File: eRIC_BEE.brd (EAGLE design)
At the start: 25.2 x 34 mm, 40 parts

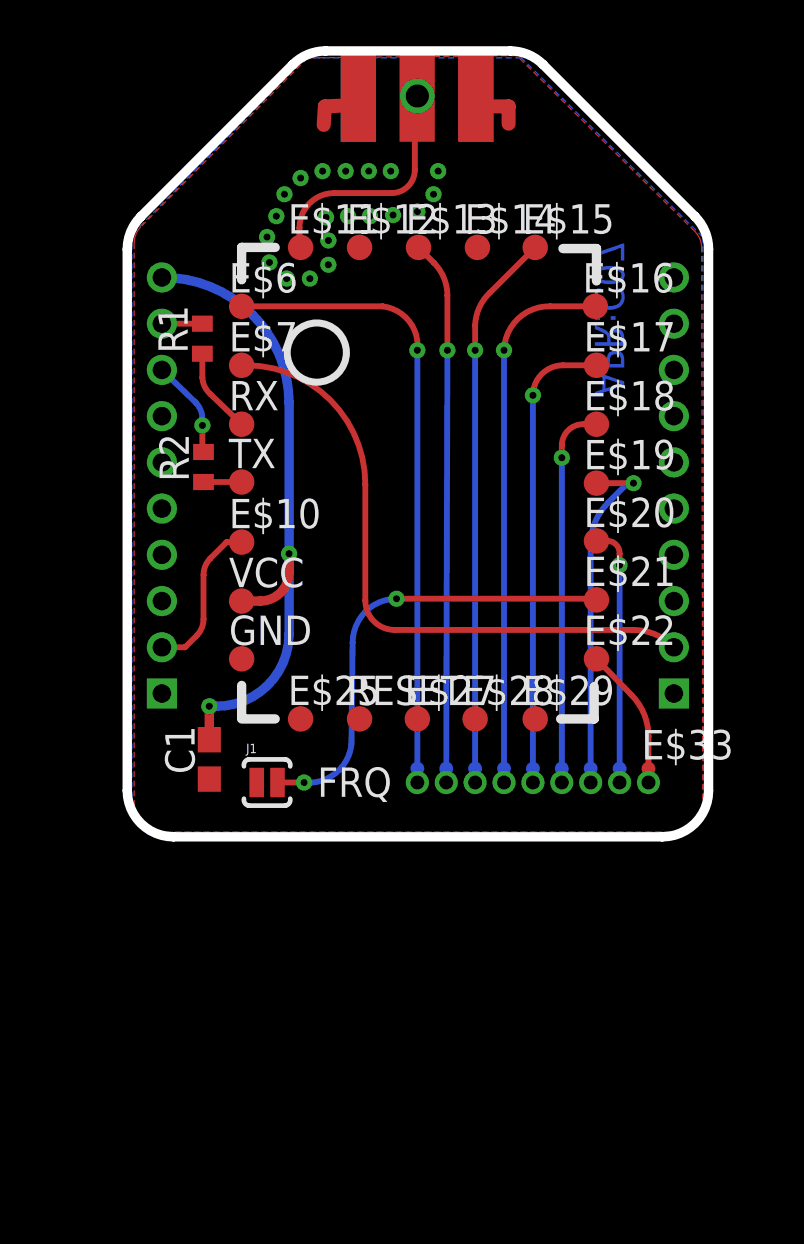
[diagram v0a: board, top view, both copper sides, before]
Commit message: revision 1.8, eagle 7.2 cam, new board design to eliminate need for wonky stitching
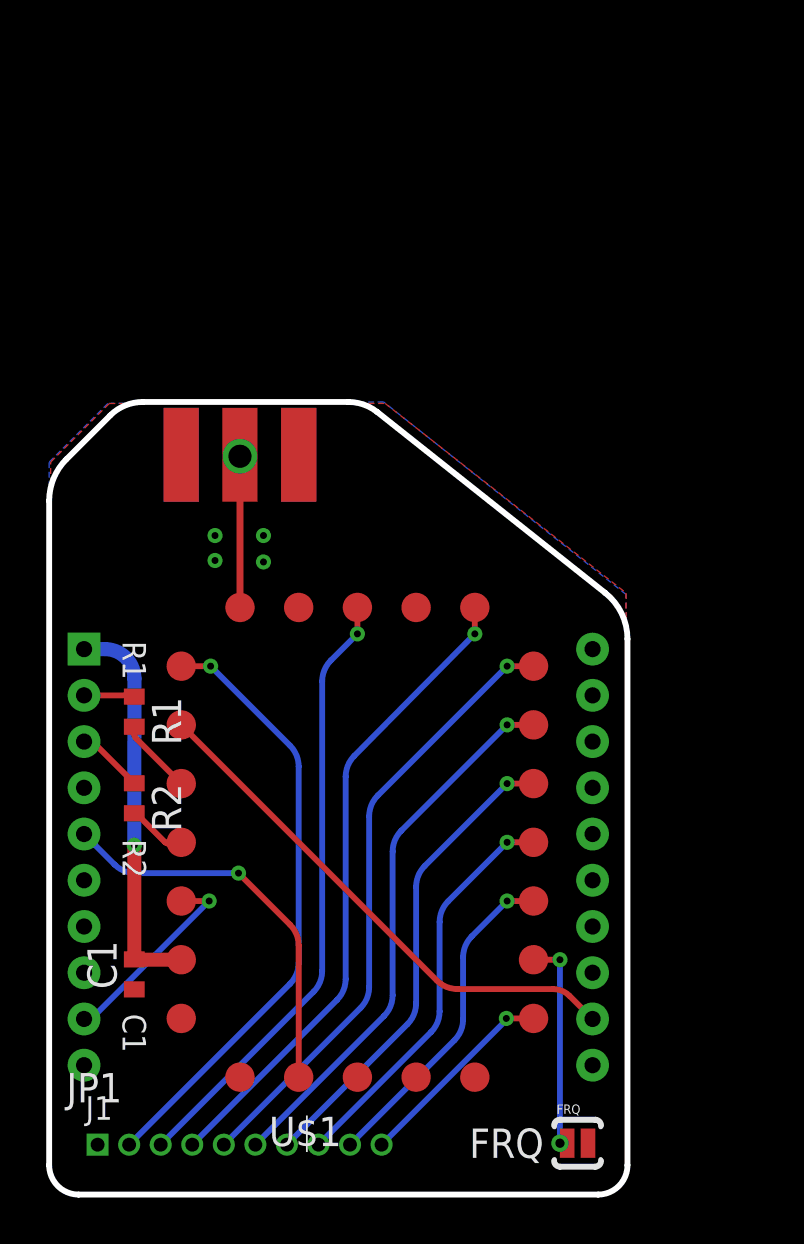
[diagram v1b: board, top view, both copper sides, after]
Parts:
- removed E$10, E$11, E$12, E$13, E$14, E$15, E$16, E$17, E$18, E$19, E$20, E$21, E$22, E$25, E$27, E$28, E$29, E$6, E$7, GND, RESET, RX, TX, VCC: (no value), testpad:TP11R
- removed E$2, E$30, E$31, E$32, E$33, E$4, E$5, E$8, E$9: (no value), testpad:TP06R
- removed H1, H2: (no value), SparkFun-Connectors:1X10-2MM
- removed J1: (no value), SparkFun-Capacitors:SJ_2S-NO
- removed SMA: (no value), SparkFun-Connectors:SMA-EDGE
- added FRQ: (no value), SparkFun-Passives:PAD-JUMPER-2-NO_YES_SILK
- added J$2: SMA_EDGE, SparkFun-Connectors:SMA-EDGE
- added JP1: M102MM, SparkFun-Connectors:1X10-2MM
- added U$1: XBEE, adafruit:XBEE
- added U1: ERIC, lprs:ERIC
- C1: value .1uF -> (none); device eagle-ltspice:C0603 -> adafruit:C0402
- R1, R2: value 10K -> (none); device ref-packages:R0402 -> adafruit:R0402
- moved R1 16.4 mm to (8.26, 20.8), turned to 270 degrees
- moved R2 14.6 mm to (8.26, 17.0), turned to 270 degrees
- moved C1 9.85 mm to (8.26, 9.40)
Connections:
- removed net ANT: E$11.TP, SMA.SIG
- removed net S$1: E$21.TP, J1.2
- removed net S$11: E$2.TP, E$6.TP
- removed net S$14: R2.1, TX.TP
- removed net S$18: E$25.TP
- removed net S$19: E$13.TP, E$4.TP
- removed net S$20: E$15.TP, E$5.TP
- removed net S$21: E$16.TP, E$8.TP
- removed net S$22: E$17.TP, E$9.TP
- removed net S$23: E$18.TP, E$30.TP
- removed net S$24: E$19.TP, E$31.TP
- removed net S$25: E$20.TP, E$32.TP
- removed net S$26: E$22.TP, E$33.TP
- removed net S$27: H1.8, R2.2
- removed net S$28: H1.9, R1.2
- removed net S$3: R1.1, RX.TP
- removed net S$6: E$10.TP, H1.2
- removed net S$7: C1.2, H1.10, VCC.TP
- removed net S$8: E$7.TP, H2.2
- new net N$1: FRQ.1, U1.FS
- new net N$10: JP1.2, U1.CD
- new net N$11: JP1.3, U1.E22
- new net N$12: JP1.5, U1.E19
- new net N$13: JP1.6, U1.E18
- new net N$14: JP1.7, U1.E17
- new net N$15: JP1.8, U1.E16
- new net N$16: JP1.9, U1.E15
- new net N$17: JP1.10, U1.E13
- new net N$18: U$1.5, U1.E9
- new net N$2: R1.1, U$1.2
- new net N$3: R2.1, U$1.3
- new net N$4: J$2.SIG, U1.ANT
- new net N$5: U$1.9, U1.HR
- new net N$6: R2.2, U1.SDI
- new net N$7: U$1.12, U1.BUSY
- new net N$8: R1.2, U1.SDO
- new net N$9: JP1.4, U1.E20
- new net VCC: C1.2, U$1.1, U1.VCC
- net GND: now also FRQ.2, J$2.GND@0, J$2.GND@1, J$2.GND@2, J$2.GND@3, JP1.1, U$1.10, U1.AGND, U1.GND; no longer E$12.TP, GND.TP, H1.1, J1.1, SMA.GND@0, SMA.GND@1, SMA.GND@2, SMA.GND@3
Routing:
- net N$9: track 0.00 -> 28.1 mm, vias 0 -> 1
- net S$7: track 27.3 -> 0.00 mm, vias 2 -> 0
- net N$12: track 0.00 -> 26.8 mm, vias 0 -> 1
- net S$11: track 26.6 -> 0.00 mm, vias 1 -> 0
- net N$11: track 0.00 -> 26.6 mm, vias 0 -> 1
- net S$8: track 26.5 -> 0.00 mm
- net N$10: track 0.00 -> 26.4 mm, vias 0 -> 1
- net N$13: track 0.00 -> 23.7 mm, vias 0 -> 1
- net S$20: track 23.5 -> 0.00 mm, vias 1 -> 0
- net S$19: track 22.9 -> 0.00 mm, vias 1 -> 0
- net N$7: track 0.00 -> 22.9 mm
- net S$21: track 22.8 -> 0.00 mm, vias 1 -> 0
- net N$14: track 0.00 -> 20.5 mm, vias 0 -> 1
- net S$1: track 19.5 -> 0.00 mm, vias 2 -> 0
- net S$22: track 19.4 -> 0.00 mm, vias 1 -> 0
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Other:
- board size 25.2 x 34 mm -> 25 x 34.3 mm
- board text added: "APR:H07"
- board text added: "C1"
- board text added: "J1"
- board text added: "R1"
- board text added: "R2"
- board text removed: "APR:C07"
